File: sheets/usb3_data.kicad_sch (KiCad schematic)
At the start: 0 parts

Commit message: sch: USB3 data port + HD3SS3220 + correct 35/37 AC caps
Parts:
- added C58, C59: 220nF, Capacitor_SMD:C_0603_1608Metric, symbol Device:C_Small
- added C60, C61: 1uF/16V, Capacitor_SMD:C_0603_1608Metric, symbol Device:C_Small
- added C62: 1nF, Capacitor_SMD:C_0603_1608Metric, symbol Device:C_Small
- added D20, D21, D22: TPD4EUSB30DQAR, Package_SON:USON-10_2.5x1.0mm_P0.5mm, symbol Power_Protection:TPD4EUSB30
- added D23: TPD4E05U06DQAR, Package_SON:USON-10_2.5x1.0mm_P0.5mm, symbol Power_Protection:TPD4E05U06DQA
- added D24: SMAJ5.0A-TR, Diode_SMB:D_SMB, symbol sierra-to-usb:SMAJ5.0A
- added J1: TYPE-C-31-M-17, Connector_USB:USB_C_Receptacle_HRO_TYPE-C-31-M-17, symbol sierra-to-usb:USB_C_Receptacle_USB3.2_24P
- added R69: 900k 1%, Resistor_SMD:R_0603_1608Metric, symbol Device:R_Small
- added R70: 1M, Resistor_SMD:R_0603_1608Metric, symbol Device:R_Small
- added R71: 200k, Resistor_SMD:R_0603_1608Metric, symbol Device:R_Small
- added U1: HD3SS3220RNHR, Package_DFN_QFN:HD3SS3220_RNH0030A, symbol sierra-to-usb:HD3SS3220
- added U4: AP2112K-3.3TRG1, Package_TO_SOT_SMD:SOT-23-5, symbol Regulator_Linear:AP2112K-3.3
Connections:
- new net +3V3_MUX: C61.1, U1.8 (VCC33), U4.5 (VOUT)
- new net CC1_RAW: D23.4 (D2+), J1.A5 (CC1), U1.2 (CC1)
- new net CC2_RAW: D23.5 (D2-), J1.B5 (CC2), U1.1 (CC2)
- new net GND: C60.2, C61.2, C62.2, D20.3 (GND), D20.8 (GND), D21.3 (GND), D21.8 (GND), D22.3 (GND), D22.8 (GND), D23.3 (GND), D23.8 (GND), D24.2 (A), J1.A1 (GND), J1.A12 (GND), J1.B1 (GND), J1.B12 (GND), R70.2, U1.12 (EN_MUX_N), U1.13 (GND), U1.28 (GND), U1.29 (EN_CC_N), U1.3 (CURRENT_MODE), U1.31 (PAD), U1.4 (PORT), U4.2 (GND)
- new net HD_VBUSDET: R69.2, U1.5 (VBUS_DET)
- new net N_J1_SHIELD: C62.1, J1.SH (SHIELD), R70.1
- new net N_TXN_PRECAP: C59.1, U1.7 (TXN)
- new net N_TXP_PRECAP: C58.1, U1.6 (TXP)
- new net N_U1_DIR: R71.1, U1.11 (DIR)
- new net SS_CON1_RXN: D20.5 (D2-), J1.B10 (SSRXN1), U1.14 (RX1N)
- new net SS_CON1_RXP: D20.4 (D2+), J1.B11 (SSRXP1), U1.15 (RX1P)
- new net SS_CON1_TXN: D20.2 (D1-), J1.A3 (SSTXN1), U1.16 (TX1N)
- new net SS_CON1_TXP: D20.1 (D1+), J1.A2 (SSTXP1), U1.17 (TX1P)
- new net SS_CON2_RXN: D21.5 (D2-), J1.A10 (SSRXN2), U1.18 (RX2N)
- new net SS_CON2_RXP: D21.4 (D2+), J1.A11 (SSRXP2), U1.19 (RX2P)
- new net SS_CON2_TXN: D21.2 (D1-), J1.B3 (SSTXN2), U1.20 (TX2N)
- new net SS_CON2_TXP: D21.1 (D1+), J1.B2 (SSTXP2), U1.21 (TX2P)
- new net SS_MOD_RX_N: D22.5 (D2-), U1.10 (RXN)
- new net SS_MOD_RX_P: D22.4 (D2+), U1.9 (RXP)
- new net SS_MOD_TX_C_N: C59.2, D22.2 (D1-)
- new net SS_MOD_TX_C_P: C58.2, D22.1 (D1+)
- new net USB2_CON_DM: D23.2 (D1-), J1.A7 (D-), J1.B7 (D-)
- new net USB2_CON_DP: D23.1 (D1+), J1.A6 (D+), J1.B6 (D+)
- new net VBUS_DATA: C60.1, D24.1 (K), J1.A4 (VBUS), J1.A9 (VBUS), J1.B4 (VBUS), J1.B9 (VBUS), R69.1, R71.2, U1.30 (VDD5), U4.1 (VIN), U4.3 (EN)
- no-connect marks 0 -> 24

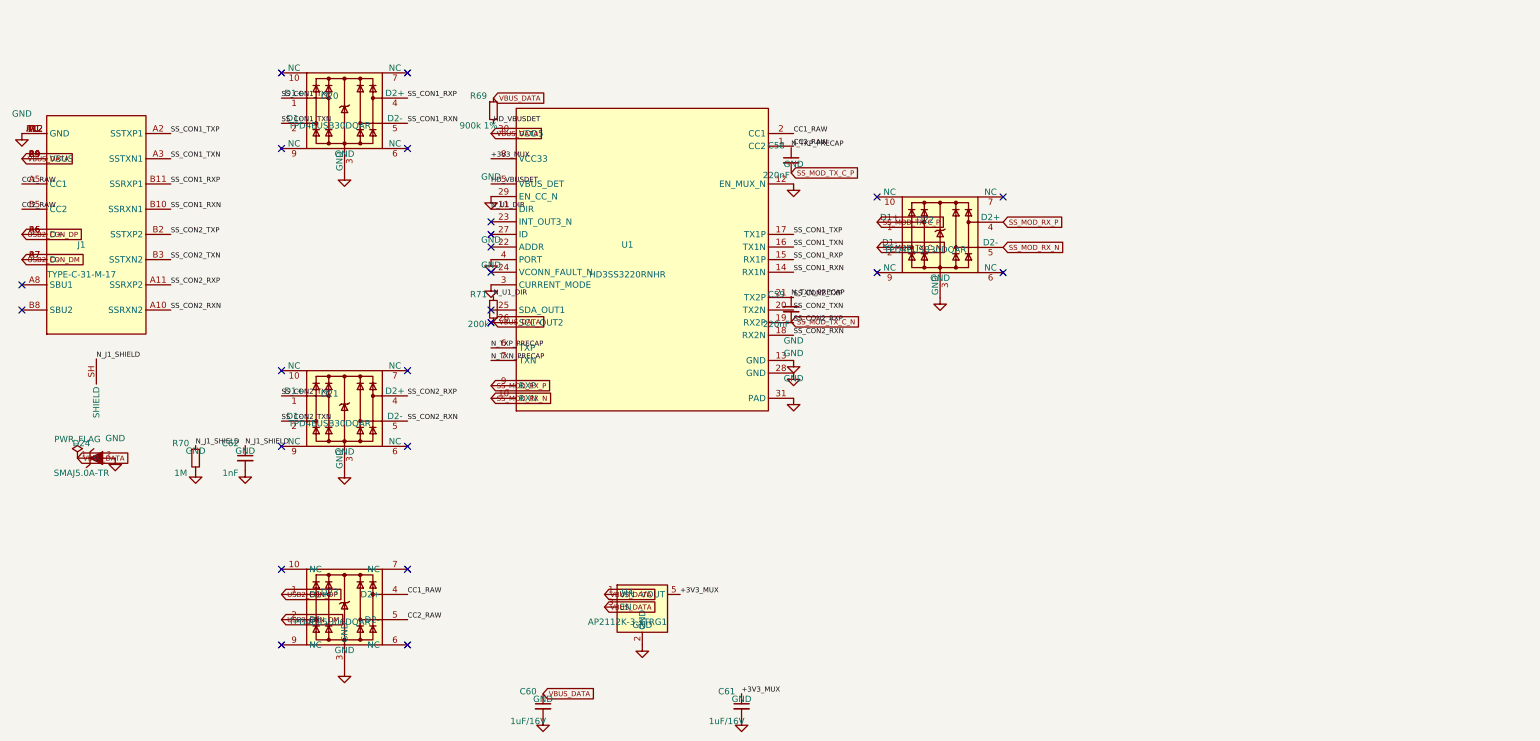
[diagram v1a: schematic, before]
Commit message: sch: usb3_data — correct HD3SS3220 module-side TX/RX roles, DIR pull-up to 3V3
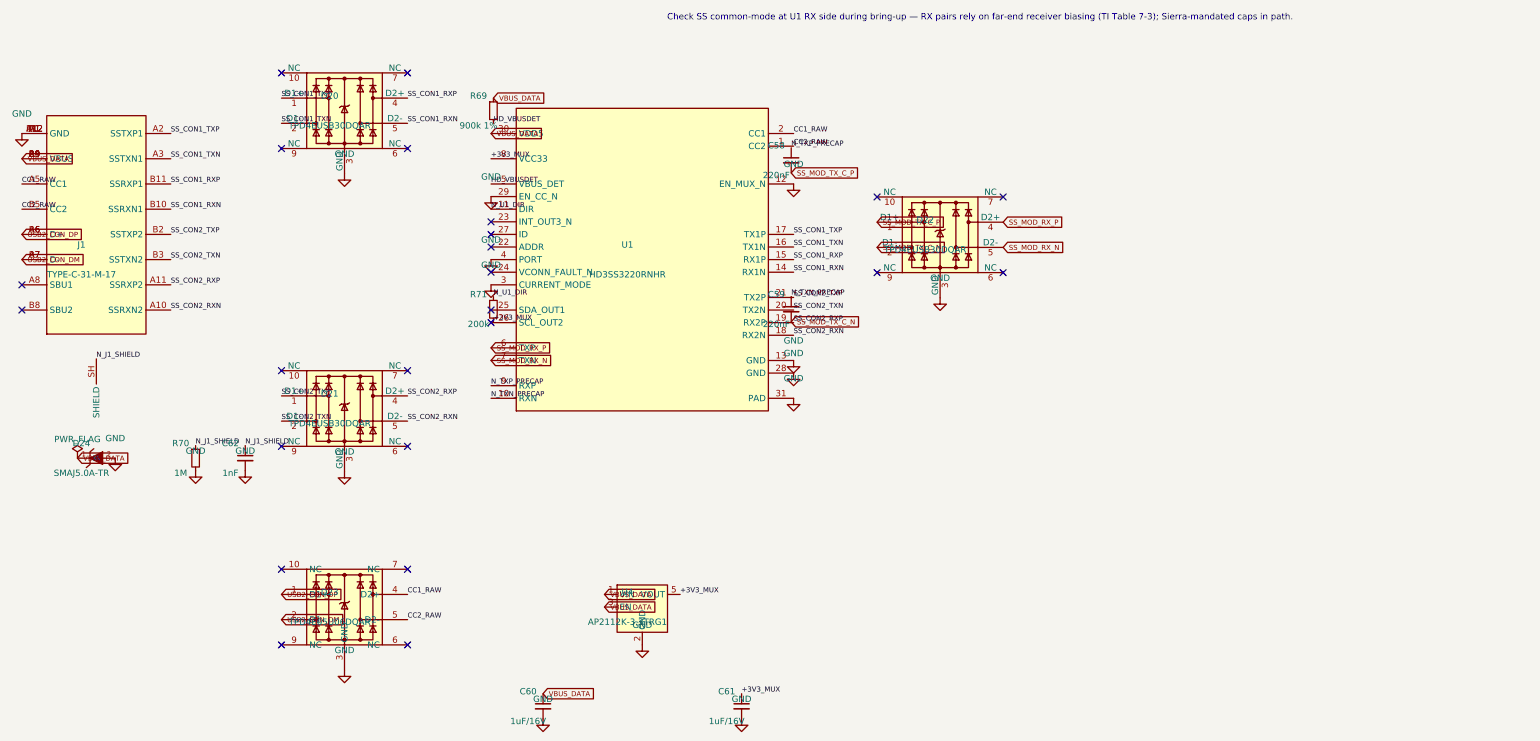
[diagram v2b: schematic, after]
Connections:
- net +3V3_MUX: now also R71.2
- net N_TXN_PRECAP: now also U1.10 (RXN); no longer U1.7 (TXN)
- net N_TXP_PRECAP: now also U1.9 (RXP); no longer U1.6 (TXP)
- net SS_MOD_RX_N: now also U1.7 (TXN); no longer U1.10 (RXN)
- net SS_MOD_RX_P: now also U1.6 (TXP); no longer U1.9 (RXP)
- net VBUS_DATA: no longer R71.2
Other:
- note added: "Check SS common-mode at U1 RX side during bring-up — RX pairs rely on far-end receiver biasing (TI Table 7-3); Sierra-mandated caps in path."
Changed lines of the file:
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@@
 	)
 	(label "N_TXP_PRECAP"
-		(at 99.52 77.78 0)
+		(at 99.52 85.4 0)
 		(effects (font (size 1.016 1.016)) (justify left bottom))
 	)
 	(label "N_TXN_PRECAP"
-		(at 99.52 80.32 0)
+		(at 99.52 87.94 0)
 		(effects (font (size 1.016 1.016)) (justify left bottom))
 	)
@@
 	(global_label "SS_MOD_RX_P"
 		(shape input)
-		(at 99.52 85.4 0)
-		(effects (font (size 1.016 1.016)) (justify left bottom))
-		(property "Intersheetrefs" "${INTERSHEET_REFS}" (at 99.52 85.4 0) (effects (font (size 1.27 1.27))))
+		(at 99.52 77.78 0)
+		(effects (font (size 1.016 1.016)) (justify left bottom))
+		(property "Intersheetrefs" "${INTERSHEET_REFS}" (at 99.52 77.78 0) (effects (font (size 1.27 1.27))))
 	)
 	(global_label "SS_MOD_RX_N"
 		(shape input)
-		(at 99.52 87.94 0)
-		(effects (font (size 1.016 1.016)) (justify left bottom))
-		(property "Intersheetrefs" "${INTERSHEET_REFS}" (at 99.52 87.94 0) (effects (font (size 1.27 1.27))))
+		(at 99.52 80.32 0)
+		(effects (font (size 1.016 1.016)) (justify left bottom))
+		(property "Intersheetrefs" "${INTERSHEET_REFS}" (at 99.52 80.32 0) (effects (font (size 1.27 1.27))))
 	)
 	(label "N_U1_DIR"
@@
 		(effects (font (size 1.016 1.016)) (justify left bottom))
 	)
-	(global_label "VBUS_DATA"
-		(shape input)
+	(label "+3V3_MUX"
 		(at 100 72.54 0)
 		(effects (font (size 1.016 1.016)) (justify left bottom))
-		(property "Intersheetrefs" "${INTERSHEET_REFS}" (at 100 72.54 0) (effects (font (size 1.27 1.27))))
 	)
 	(symbol
@@
 		)
 	)
+	(text "Check SS common-mode at U1 RX side during bring-up — RX pairs rely on far-end receiver biasing (TI Table 7-3); Sierra-mandated caps in path."
+		(exclude_from_sim no)
+		(at 135 12 0)
+		(effects (font (size 1.27 1.27)) (justify left bottom))
+	)
 	(sheet_instances
